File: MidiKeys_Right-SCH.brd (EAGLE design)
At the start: 100 x 80 mm, 112 parts

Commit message: regenerated board
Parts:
- renumbered U$1 to A2, U$10 to B3B, U$11 to B4, U$12 to B4B, U$13 to C2, U$14 to C3, U$15 to C4, U$16 to C5, U$17 to D2, U$18 to D2B, U$19 to D3, U$2 to A2B, U$20 to D3B, U$21 to D4, U$22 to D4B, U$23 to E2, U$24 to E2B, U$25 to E3, U$26 to E3B, U$27 to E4, U$28 to E4B, U$29 to F2, U$3 to A3, U$30 to F3, U$31 to F4, U$32 to G2, U$33 to G2B, U$34 to G3, U$35 to G3B, U$36 to G4, U$37 to G4B, U$4 to A3B, U$5 to A4, U$6 to A4B, U$7 to B2, U$8 to B2B, U$9 to B3
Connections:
- net KEY_A2: now also A2.SW1; no longer B2.SW1
- net KEY_A2B: now also A2B.SW1; no longer E3B.SW1
- net KEY_A3: now also A3.SW1; no longer C3.SW1
- net KEY_A3B: now also A3B.SW1; no longer F4.SW1
- net KEY_A4: now also A4.SW1; no longer D4.SW1
- net KEY_A4B: now also A4B.SW1; no longer G4.SW1
- net KEY_B2: now also B2.SW1; no longer B2B.SW1
- net KEY_B2B: now also B2B.SW1; no longer E4.SW1
- net KEY_B3: now also B3.SW1; no longer C4.SW1
- net KEY_B3B: now also B3B.SW1; no longer G2.SW1
- net KEY_B4: now also B4.SW1; no longer D4B.SW1
- net KEY_B4B: now also B4B.SW1; no longer G4B.SW1
- net KEY_C2: now also C2.SW1; no longer A2.SW1
- net KEY_C3: now also C3.SW1; no longer B3.SW1
- net KEY_C4: now also C4.SW1; no longer C5.SW1
- net KEY_C5: now also C5.SW1; no longer E2.SW1
- net KEY_D2: now also D2.SW1; no longer A3.SW1
- net KEY_D2B: now also D2B.SW1; no longer A2B.SW1
- net KEY_D3: now also D3.SW1; no longer B3B.SW1
- net KEY_D3B: now also D3B.SW1; no longer E4B.SW1
- net KEY_D4: now also D4.SW1; no longer D2.SW1
- net KEY_D4B: now also D4B.SW1; no longer G2B.SW1
- net KEY_E2: now also E2.SW1; no longer A3B.SW1
- net KEY_E3: now also E3.SW1; no longer B4.SW1
- net KEY_E3B: now also E3B.SW1; no longer F2.SW1
- net KEY_E4: now also E4.SW1; no longer D2B.SW1
- net KEY_E4B: now also E4B.SW1; no longer G3.SW1
- net KEY_F2: now also F2.SW1; no longer A4.SW1
- net KEY_F3: now also F3.SW1; no longer B4B.SW1
- net KEY_F4: now also F4.SW1; no longer D3.SW1
- net KEY_G2: now also G2.SW1; no longer A4B.SW1
- net KEY_G2B: now also G2B.SW1; no longer E3.SW1
- net KEY_G3: now also G3.SW1; no longer C2.SW1
- net KEY_G3B: now also G3B.SW1; no longer F3.SW1
- net KEY_G4: now also G4.SW1; no longer D3B.SW1
- net KEY_G4B: now also G4B.SW1; no longer G3B.SW1
- net N$1: now also D2.LED+; no longer A3.LED+
- net N$10: now also D3.LED+; no longer B3B.LED+
- net N$11: now also E3.LED+; no longer B4.LED+
- net N$12: now also F3.LED+; no longer B4B.LED+
- net N$13: now also G3.LED+; no longer C2.LED+
- net N$14: now also A3.LED+; no longer C3.LED+
- net N$15: now also B3.LED+; no longer C4.LED+
- net N$16: now also C4.LED+; no longer C5.LED+
- net N$17: now also D4.LED+; no longer D2.LED+
- net N$18: now also E4.LED+; no longer D2B.LED+
- net N$19: now also F4.LED+; no longer D3.LED+
- net N$2: now also E2.LED+; no longer A3B.LED+
- net N$20: now also G4.LED+; no longer D3B.LED+
- net N$21: now also A4.LED+; no longer D4.LED+
- net N$22: now also B4.LED+; no longer D4B.LED+
- net N$23: now also C5.LED+; no longer E2.LED+
- net N$25: now also G2B.LED+; no longer E3.LED+
- net N$26: now also A2B.LED+; no longer E3B.LED+
- net N$27: now also B2B.LED+; no longer E4.LED+
- net N$28: now also D3B.LED+; no longer E4B.LED+
- net N$29: now also E3B.LED+; no longer F2.LED+
- net N$3: now also F2.LED+; no longer A4.LED+
- net N$30: now also G3B.LED+; no longer F3.LED+
- net N$31: now also A3B.LED+; no longer F4.LED+
- net N$32: now also B3B.LED+; no longer G2.LED+
- net N$33: now also D4B.LED+; no longer G2B.LED+
- net N$34: now also E4B.LED+; no longer G3.LED+
- net N$35: now also G4B.LED+; no longer G3B.LED+
- net N$36: now also A4B.LED+; no longer G4.LED+
- net N$37: now also B4B.LED+; no longer G4B.LED+
- net N$4: now also D2B.LED+; no longer A2B.LED+
- net N$5: now also C2.LED+; no longer A2.LED+
- net N$6: now also G2.LED+; no longer A4B.LED+
- net N$7: now also A2.LED+; no longer B2.LED+
- net N$8: now also B2.LED+; no longer B2B.LED+
- net N$9: now also C3.LED+; no longer B3.LED+

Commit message: updated switch library part
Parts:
- moved G4B 925.9 mm to (-5.08, -795.0)
- moved B4B 921.3 mm to (-5.08, -840.7)
- moved E4B 885.8 mm to (-5.08, -772.2)
- moved A4B 883.9 mm to (-5.08, -817.9)
- moved D4B 848.4 mm to (-5.08, -749.3)
- moved G3B 810.4 mm to (-5.08, -680.7)
- moved B3B 800.9 mm to (-5.08, -726.4)
- moved A3B 767.8 mm to (-5.08, -703.6)
- moved E3B 765.9 mm to (-5.08, -657.9)
- moved D3B 732.3 mm to (-5.08, -635.0)
- moved G2B 689.2 mm to (-5.08, -566.4)
- moved B2B 682.9 mm to (-5.08, -612.1)
- moved E2B 647.7 mm to (-5.08, -543.6)
- moved A2B 613.4 mm to (-5.08, -589.3)
- moved C5 608.8 mm to (-5.08, -520.7)
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
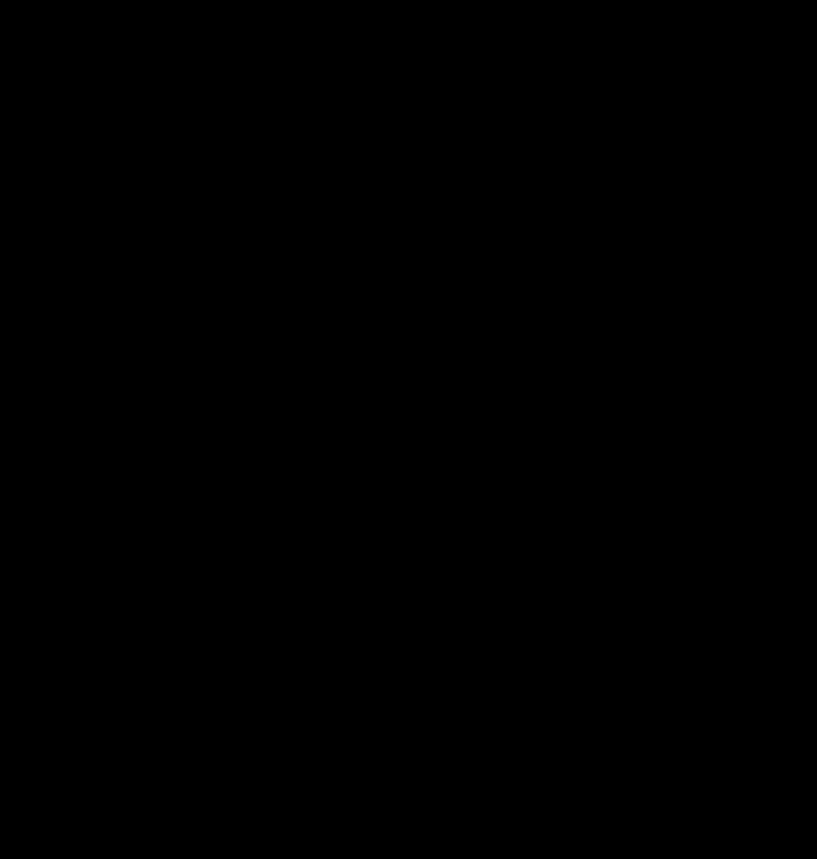
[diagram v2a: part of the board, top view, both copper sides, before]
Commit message: added transistor led driver circuit@
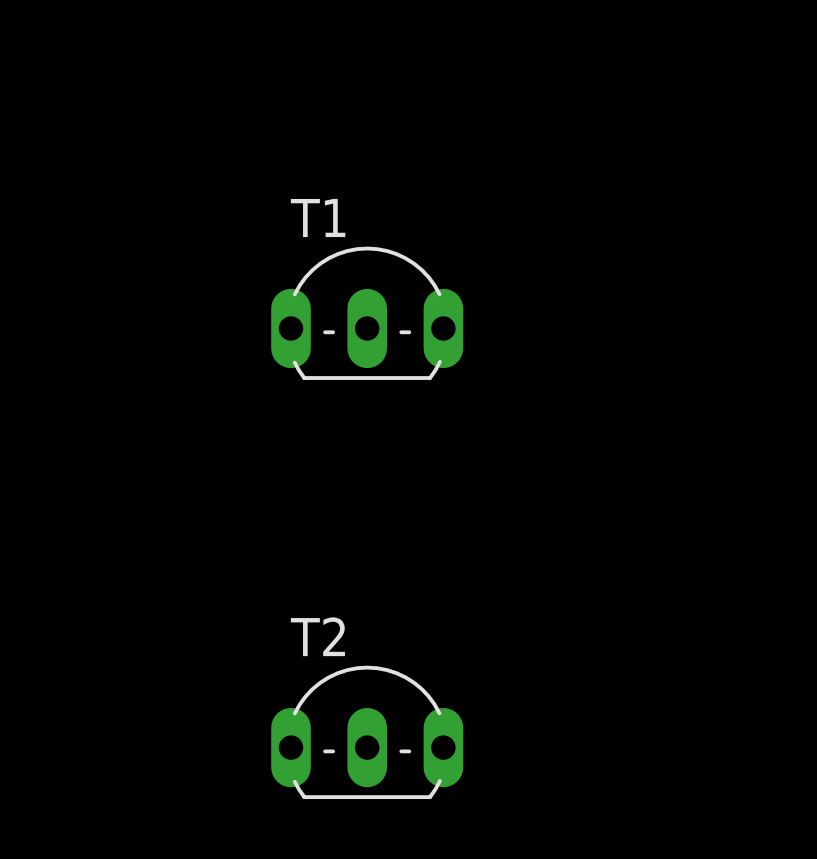
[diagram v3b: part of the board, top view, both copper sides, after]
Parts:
- added T1, T2: 2N2222, adafruit:TO92-EBC-OVAL
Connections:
- removed net LED_BOTTOM_CNTRL: ARDUINO_DUE1.2, R10.2, R12.2, R14.2, R16.2, R18.2, R20.2, R22.2, R24.2, R26.2, R28.2, R3.2, R30.2, R32.2, R34.2, R36.2, R38.2, R40.2, R42.2, R44.2, R46.2, R6.2, R8.2
- removed net LED_TOP_CNTRL: ARDUINO_DUE1.3, R4.2, R48.2, R50.2, R52.2, R54.2, R56.2, R58.2, R60.2, R62.2, R64.2, R66.2, R68.2, R70.2, R72.2, R74.2
- new net LED_CNTRL_BOTTOM: ARDUINO_DUE1.2, T1.B
- new net LED_CNTRL_TOP: ARDUINO_DUE1.3, T2.B
- net GND: now also T2.E
- net VCC: now also R10.2, R12.2, R14.2, R16.2, R18.2, R20.2, R22.2, R24.2, R26.2, R28.2, R3.2, R30.2, R32.2, R34.2, R36.2, R38.2, R4.2, R40.2, R42.2, R44.2, R46.2, R48.2, R50.2, R52.2, R54.2, R56.2, R58.2, R6.2, R60.2, R62.2, R64.2, R66.2, R68.2, R70.2, R72.2, R74.2, R8.2; no longer R47.2, R49.2, R51.2, R53.2, R69.2, R71.2, R73.2

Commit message: synced board to schematic
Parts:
- added R75, R76: 1K65, resistor:R0603
- R10, R12, R14, R16, R18, R20, R22, R24, R26, R28, R3, R30, R32, R34, R36, R38, R4, R40, R42, R44, R46, R48, R50, R52, R54, R56, R58, R6, R60, R62, R64, R66, R68, R70, R72, R74, R8: value 220R -> 82R
- moved T2 1009.0 mm to (-76.2, 132.1)
- moved T1 995.7 mm to (-67.3, 132.1)
- moved G4B 931.0 mm to (-54.6, 134.6)
- moved B4B 922.6 mm to (-38.1, 81.3)
- moved E4B 889.6 mm to (-38.1, 116.8)
- moved A4B 883.9 mm to (-71.1, 63.5)
- moved D4B 850.9 mm to (-71.1, 99.1)
- moved G3B 815.5 mm to (-21.6, 134.6)
- moved B3B 800.9 mm to (-137.2, 63.5)
- moved E3B 768.4 mm to (-137.2, 99.1)
- moved A3B 767.8 mm to (-38.1, 63.5)
- moved D3B 734.8 mm to (-38.1, 99.1)
- moved G2B 693.0 mm to (-120.7, 116.8)
- moved B2B 682.9 mm to (-104.1, 63.5)
- moved E2B 650.2 mm to (-104.1, 99.1)
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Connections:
- new net N$65: A2B.LED-, A3B.LED-, A4B.LED-, B2B.LED-, B3B.LED-, B4B.LED-, D2B.LED-, D3B.LED-, D4B.LED-, E2B.LED-, E3B.LED-, E4B.LED-, G2B.LED-, G3B.LED-, G4B.LED-, T2.C
- new net N$74: A2.LED-, A3.LED-, A4.LED-, B2.LED-, B3.LED-, B4.LED-, C2.LED-, C3.LED-, C4.LED-, C5.LED-, D2.LED-, D3.LED-, D4.LED-, E2.LED-, E3.LED-, E4.LED-, F2.LED-, F3.LED-, F4.LED-, G2.LED-, G3.LED-, G4.LED-, T1.C
- new net N$75: R75.2, T2.B
- new net N$76: R76.2, T1.B
- net GND: now also T1.E; no longer A2.LED-, A2B.LED-, A3.LED-, A3B.LED-, A4.LED-, A4B.LED-, B2.LED-, B2B.LED-, B3.LED-, B3B.LED-, B4.LED-, B4B.LED-, C2.LED-, C3.LED-, C4.LED-, C5.LED-, D2.LED-, D2B.LED-, D3.LED-, D3B.LED-, D4.LED-, D4B.LED-, E2.LED-, E2B.LED-, E3.LED-, E3B.LED-, E4.LED-, E4B.LED-, F2.LED-, F3.LED-, F4.LED-, G2.LED-, G2B.LED-, G3.LED-, G3B.LED-, G4.LED-, G4B.LED-
- net LED_CNTRL_BOTTOM: now also R76.1; no longer T1.B
- net LED_CNTRL_TOP: now also R75.1; no longer T2.B
- net VCC: now also R47.2, R49.2, R51.2, R53.2, R69.2, R71.2, R73.2

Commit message: added OSH Park drc and cam plugin to eagle and updated board outline to required dimensions
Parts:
- moved ARDUINO_DUE1 106.0 mm to (-9.57, 2.27)
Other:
- board size 100 x 80 mm -> 550 x 60 mm

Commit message: removed arduino shield and transistors. added 50way idc connector and solder bridges to manually connect up the correct octave. board size now 140x60. sch done. layout started
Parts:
- removed A3, A3B, A4, A4B, B3, B3B, B4, B4B, C3, C4, C5, D3, D3B, D4, D4B, E3, E3B, E4, E4B, F3, F4, G3, G3B, G4, G4B: CHERRY-MX-LED, cherrymx:CHERRY-MX-LED
- removed ARDUINO_DUE1: U1, arduino_due_shield:ARDUINO_DUE_SHIELD
- removed R17, R19, R21, R23, R25, R27, R29, R31, R33, R35, R37, R39, R41, R43, R45, R55, R57, R59, R61, R63, R65, R67, R69, R71, R73: 10k, resistor:R0603
- removed R18, R20, R22, R24, R26, R28, R30, R32, R34, R36, R38, R40, R42, R44, R46, R56, R58, R60, R62, R64, R66, R68, R70, R72, R74: 82R, resistor:R0603
- removed R75, R76: 1K65, resistor:R0603
- removed T1, T2: 2N2222, adafruit:TO92-EBC-OVAL
- added J1: (no value), con-3m-skt-header:S50V
- added SA2, SA2B, SA3, SA3B, SA4, SA4B, SB2, SB2B, SB3, SB3B, SB4, SB4B, SC2, SC3, SC4, SD2, SD2B, SD3, SD3B, SD4, SD4B, SE2, SE2B, SE3, SE3B, SE4, SE4B, SF2, SF3, SF4, SG2, SG2B, SG3, SG3B, SG4, SG4B: (no value), jumper:SJ
- moved A2B 244.5 mm to (100.0, 50.0)
- moved A2 234.5 mm to (110.0, 10.0)
- moved B2B 224.5 mm to (120.0, 50.0)
- moved B2 224.1 mm to (130.0, 10.0)
- moved G2 221.6 mm to (90.0, 10.0)
- moved G2B 211.5 mm to (80.0, 50.0)
- moved D2 166.7 mm to (30.0, 10.0)
- moved F2 164.1 mm to (70.0, 10.0)
- moved E2 163.9 mm to (50.0, 10.0)
- moved D2B 160.2 mm to (20.0, 50.0)
- moved E2B 152.3 mm to (40.0, 50.0)
- moved C2 96.2 mm to (10.0, 10.0)
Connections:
- removed net KEY_C5: ARDUINO_DUE1.9, C5.SW1, R45.1
- removed net LED_CNTRL_BOTTOM: ARDUINO_DUE1.2, R76.1
- removed net LED_CNTRL_TOP: ARDUINO_DUE1.3, R75.1
- removed net N$10: D3.LED+, R20.1
- removed net N$11: E3.LED+, R22.1
- removed net N$12: F3.LED+, R24.1
- removed net N$13: G3.LED+, R26.1
- removed net N$14: A3.LED+, R28.1
- removed net N$15: B3.LED+, R30.1
- removed net N$16: C4.LED+, R32.1
- removed net N$17: D4.LED+, R34.1
- removed net N$18: E4.LED+, R36.1
- removed net N$19: F4.LED+, R38.1
- removed net N$20: G4.LED+, R40.1
- removed net N$22: B4.LED+, R44.1
- removed net N$23: C5.LED+, R46.1
- removed net N$28: D3B.LED+, R56.1
- removed net N$29: E3B.LED+, R58.1
- removed net N$30: G3B.LED+, R60.1
- removed net N$31: A3B.LED+, R62.1
- removed net N$32: B3B.LED+, R64.1
- removed net N$33: D4B.LED+, R66.1
- removed net N$34: E4B.LED+, R68.1
- removed net N$35: G4B.LED+, R70.1
- removed net N$36: A4B.LED+, R72.1
- removed net N$37: B4B.LED+, R74.1
- removed net N$65: A2B.LED-, A3B.LED-, A4B.LED-, B2B.LED-, B3B.LED-, B4B.LED-, D2B.LED-, D3B.LED-, D4B.LED-, E2B.LED-, E3B.LED-, E4B.LED-, G2B.LED-, G3B.LED-, G4B.LED-, T2.C
- removed net N$74: A2.LED-, A3.LED-, A4.LED-, B2.LED-, B3.LED-, B4.LED-, C2.LED-, C3.LED-, C4.LED-, C5.LED-, D2.LED-, D3.LED-, D4.LED-, E2.LED-, E3.LED-, E4.LED-, F2.LED-, F3.LED-, F4.LED-, G2.LED-, G3.LED-, G4.LED-, T1.C
- removed net N$75: R75.2, T2.B
- removed net N$76: R76.2, T1.B
- removed net N$9: C3.LED+, R18.1
- new net KEY_A: A2.SW1, R13.1, SA2.1, SA4.1
- new net KEY_AB: A2B.SW1, R51.1, SA2B.1, SA4B.1
- new net KEY_B: B2.SW1, R15.1, SB2.1, SB4.1
- new net KEY_BB: B2B.SW1, R53.1, SB2B.1, SB4B.1
- new net KEY_C: C2.SW1, R1.1, SC2.1, SC3.1, SC4.1
- new net KEY_D: D2.SW1, R5.1, SD2.1, SD4.1
- new net KEY_DB: D2B.SW1, R2.1, SD2B.1, SD3B.1, SD4B.1
- new net KEY_E: E2.SW1, R7.1, SE2.1, SE4.1
- new net KEY_EB: E2B.SW1, R47.1, SE2B.1, SE4B.1
- new net KEY_F: F2.SW1, R9.1, SF2.1, SF4.1
- new net KEY_G: G2.SW1, R11.1, SG2.1, SG4.1
- new net KEY_GB: G2B.SW1, R49.1, SG2B.1, SG4B.1
- new net LED_SINK_BOTTOM: A2.LED-, B2.LED-, C2.LED-, D2.LED-, E2.LED-, F2.LED-, G2.LED-, J1.30
- new net LED_SINK_TOP: A2B.LED-, B2B.LED-, D2B.LED-, E2B.LED-, G2B.LED-, J1.27
- net GND: now also J1.19, J1.21, J1.23, J1.25, J1.28; no longer A3.SW2, A3B.SW2, A4.SW2, A4B.SW2, ARDUINO_DUE1.GND, B3.SW2, B3B.SW2, B4.SW2, B4B.SW2, C3.SW2, C4.SW2, C5.SW2, D3.SW2, D3B.SW2, D4.SW2, D4B.SW2, E3.SW2, E3B.SW2, E4.SW2, E4B.SW2, F3.SW2, F4.SW2, G3.SW2, G3B.SW2, G4.SW2, G4B.SW2, T1.E, T2.E
- net KEY_A2: now also J1.12, SA2.2; no longer A2.SW1, ARDUINO_DUE1.44, R13.1
- net KEY_A2B: now also J1.11, SA2B.2; no longer A2B.SW1, ARDUINO_DUE1.45, R51.1
- net KEY_A3: now also J1.10, SA3.2; no longer A3.SW1, ARDUINO_DUE1.32, R27.1
- net KEY_A3B: now also J1.9, SA3B.2; no longer A3B.SW1, ARDUINO_DUE1.33, R61.1
- net KEY_A4: now also J1.8, SA4.2; no longer A4.SW1, ARDUINO_DUE1.12, R41.1
- net KEY_A4B: now also J1.7, SA4B.2; no longer A4B.SW1, ARDUINO_DUE1.13, R71.1
- net KEY_B2: now also J1.6, SB2.2; no longer ARDUINO_DUE1.42, B2.SW1, R15.1
- net KEY_B2B: now also J1.5, SB2B.2; no longer ARDUINO_DUE1.43, B2B.SW1, R53.1
- net KEY_B3: now also J1.4, SB3.2; no longer ARDUINO_DUE1.30, B3.SW1, R29.1
- net KEY_B3B: now also J1.3, SB3B.2; no longer ARDUINO_DUE1.31, B3B.SW1, R63.1
- net KEY_B4: now also J1.2, SB4.2; no longer ARDUINO_DUE1.10, B4.SW1, R43.1
- net KEY_B4B: now also J1.1, SB4B.2; no longer ARDUINO_DUE1.11, B4B.SW1, R73.1
- net KEY_C2: now also J1.50, SC2.2; no longer ARDUINO_DUE1.53, C2.SW1, R1.1
- net KEY_C3: now also J1.48, SC3.2; no longer ARDUINO_DUE1.41, C3.SW1, R17.1
- net KEY_C4: now also J1.46, SC4.2; no longer ARDUINO_DUE1.29, C4.SW1, R31.1
- net KEY_D2: now also J1.44, SD2.2; no longer ARDUINO_DUE1.51, D2.SW1, R5.1
- net KEY_D2B: now also J1.49, SD2B.2; no longer ARDUINO_DUE1.52, D2B.SW1, R2.1
- net KEY_D3: now also J1.42, SD3.2; no longer ARDUINO_DUE1.39, D3.SW1, R19.1
- net KEY_D3B: now also J1.47, SD3B.2; no longer ARDUINO_DUE1.40, D3B.SW1, R55.1
- net KEY_D4: now also J1.40, SD4.2; no longer ARDUINO_DUE1.27, D4.SW1, R33.1
- net KEY_D4B: now also J1.45, SD4B.2; no longer ARDUINO_DUE1.28, D4B.SW1, R65.1
- net KEY_E2: now also J1.38, SE2.2; no longer ARDUINO_DUE1.49, E2.SW1, R7.1
- net KEY_E2B: now also J1.43, SE2B.2; no longer ARDUINO_DUE1.50, E2B.SW1, R47.1
- net KEY_E3: now also J1.36, SE3.2; no longer ARDUINO_DUE1.37, E3.SW1, R21.1
- net KEY_E3B: now also J1.41, SE3B.2; no longer ARDUINO_DUE1.38, E3B.SW1, R57.1
- net KEY_E4: now also J1.34, SE4.2; no longer ARDUINO_DUE1.25, E4.SW1, R35.1
- net KEY_E4B: now also J1.39, SE4B.2; no longer ARDUINO_DUE1.26, E4B.SW1, R67.1
- net KEY_F2: now also J1.24, SF2.2; no longer ARDUINO_DUE1.48, F2.SW1, R9.1
- net KEY_F3: now also J1.22, SF3.2; no longer ARDUINO_DUE1.36, F3.SW1, R23.1
- net KEY_F4: now also J1.20, SF4.2; no longer ARDUINO_DUE1.24, F4.SW1, R37.1
- net KEY_G2: now also J1.18, SG2.2; no longer ARDUINO_DUE1.46, G2.SW1, R11.1
- net KEY_G2B: now also J1.17, SG2B.2; no longer ARDUINO_DUE1.47, G2B.SW1, R49.1
- net KEY_G3: now also J1.16, SG3.2; no longer ARDUINO_DUE1.34, G3.SW1, R25.1
- net KEY_G3B: now also J1.15, SG3B.2; no longer ARDUINO_DUE1.35, G3B.SW1, R59.1
- net KEY_G4: now also J1.14, SG4.2; no longer ARDUINO_DUE1.22, G4.SW1, R39.1
- net KEY_G4B: now also J1.13, SG4B.2; no longer ARDUINO_DUE1.23, G4B.SW1, R69.1
- net N$21: now also J1.26; no longer A4.LED+, R42.1
- net VCC: now also J1.29, J1.31, J1.32, J1.33, J1.35, J1.37; no longer ARDUINO_DUE1.3V3, R17.2, R18.2, R19.2, R20.2, R21.2, R22.2, R23.2, R24.2, R25.2, R26.2, R27.2, R28.2, R29.2, R30.2, R31.2, R32.2, R33.2, R34.2, R35.2, R36.2, R37.2, R38.2, R39.2, R40.2, R41.2, R42.2, R43.2, R44.2, R45.2, R46.2, R55.2, R56.2, R57.2, R58.2, R59.2, R60.2, R61.2, R62.2, R63.2, R64.2, R65.2, R66.2, R67.2, R68.2, R69.2, R70.2, R71.2, R72.2, R73.2, R74.2
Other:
- board size 550 x 60 mm -> 140 x 60 mm

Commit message: fixed all ERC errors and started layout.
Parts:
- J1: value (none) -> 3M 8550-4500
- moved R54 220.5 mm to (127.8, 33.7)
- moved SC4 182.8 mm to (17.0, 20.0), flipped to the bottom, turned to 90 degrees
- moved SC3 177.1 mm to (13.0, 20.0), flipped to the bottom, turned to 90 degrees
- moved SC2 171.6 mm to (9.00, 20.0), flipped to the bottom, turned to 90 degrees
- moved R3 160.0 mm to (4.00, 4.00), flipped to the bottom
- moved R1 148.4 mm to (4.00, 16.0), flipped to the bottom
- moved R2 125.4 mm to (8.17, 43.0)
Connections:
- removed net N$21: J1.26
- net GND: now also J1.26
- net KEY_A: now also SA3.1
- net KEY_AB: now also SA3B.1
- net KEY_B: now also SB3.1
- net KEY_BB: now also SB3B.1
- net KEY_D: now also SD3.1
- net KEY_E: now also SE3.1
- net KEY_EB: now also SE3B.1
- net KEY_F: now also SF3.1
- net KEY_G: now also SG3.1
- net KEY_GB: now also SG3B.1
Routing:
- net LED_SINK_BOTTOM: track 0.00 -> 133.0 mm
- net KEY_C2: track 0.00 -> 36.3 mm
- net KEY_C3: track 0.00 -> 34.3 mm
- net KEY_C4: track 0.00 -> 32.2 mm
- net KEY_C: track 0.00 -> 20.0 mm
- net N$5: track 0.00 -> 4.26 mm
